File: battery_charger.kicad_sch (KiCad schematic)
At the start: 9 parts, among them U7 BQ25185

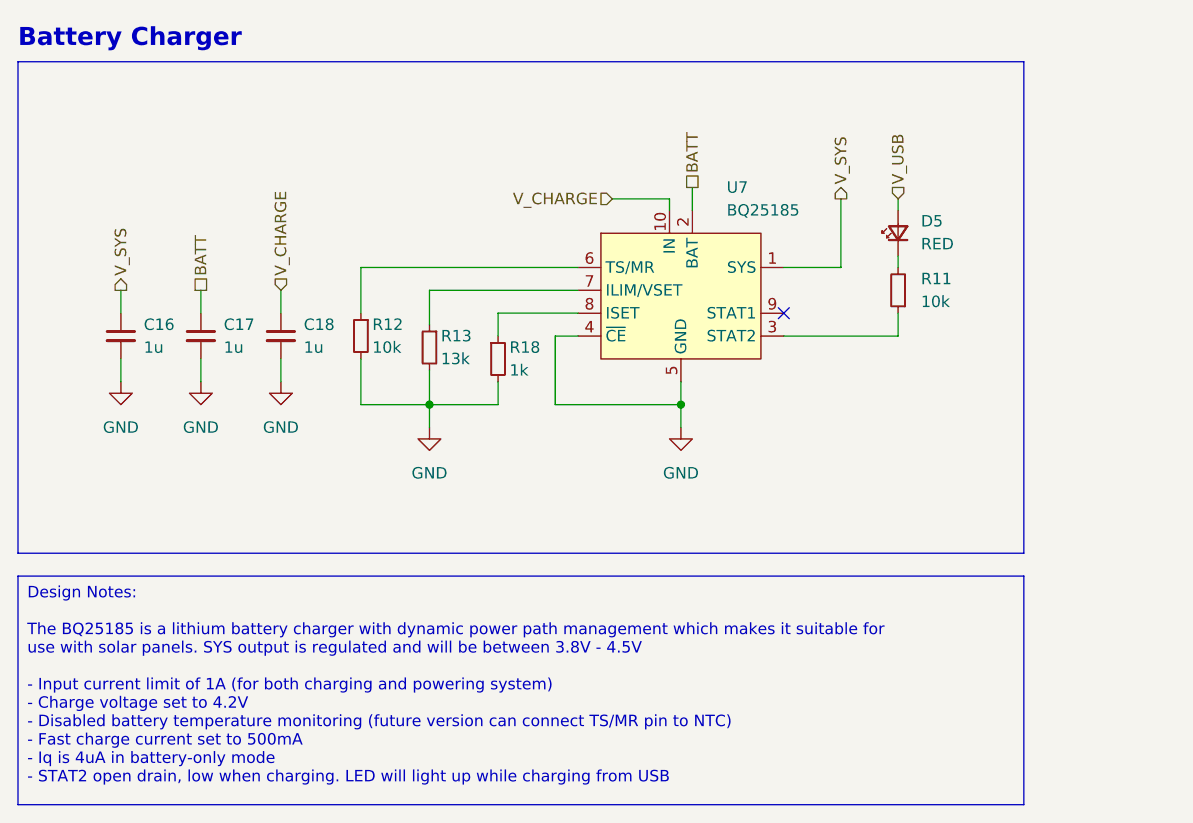
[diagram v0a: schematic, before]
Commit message: update to kicad 9.0
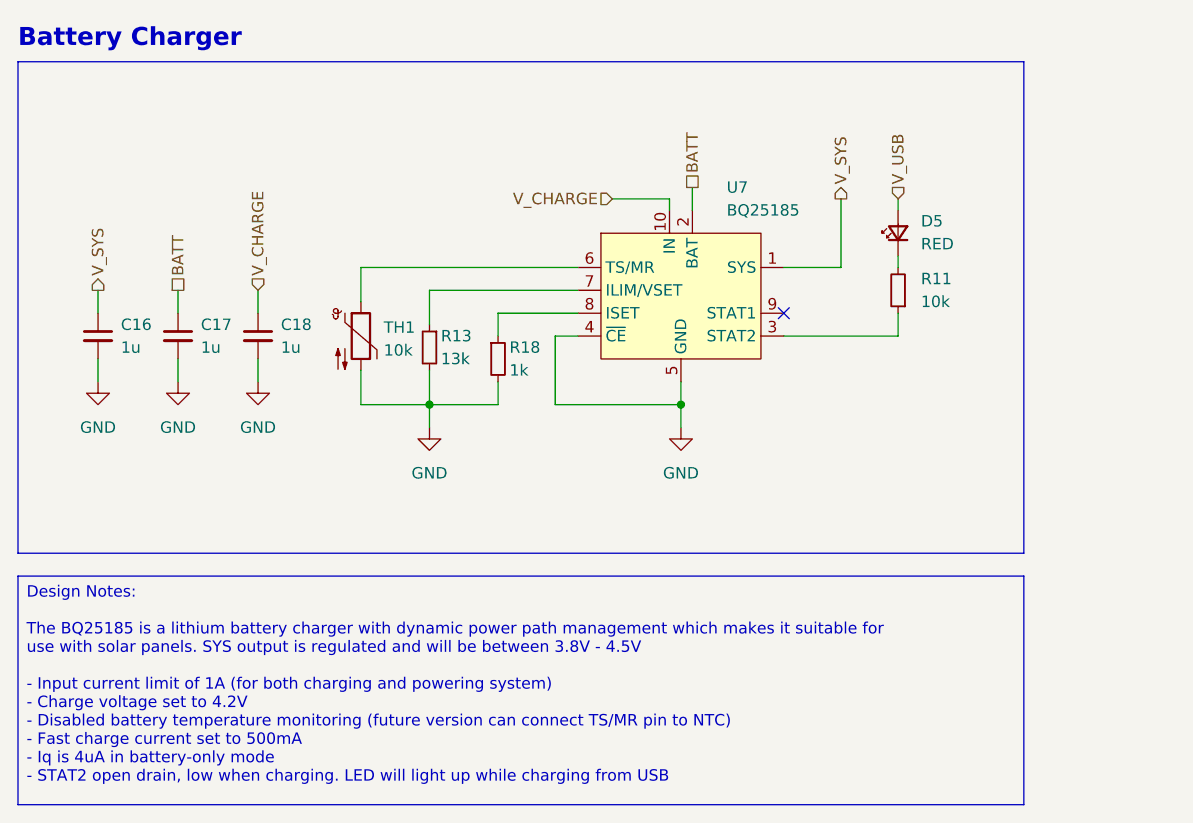
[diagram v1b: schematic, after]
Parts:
- removed R12: 10k, Resistor_SMD:R_0402_1005Metric, symbol Device:R_Small
- added TH1: 10k, Resistor_SMD:R_0402_1005Metric, symbol Device:Thermistor_NTC
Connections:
- net GND: now also TH1.2
- net at U7.6 (TS/MR): now also TH1.1
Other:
- moved on the sheet: C16, C17, C18
